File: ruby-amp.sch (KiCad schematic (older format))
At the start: 22 parts, among them J1 AudioJack3_Switch, J2 AudioJack2_Dual_Ground_Switch, P1 10k, P2 100K, P3 1k Lin, Q1 MPF102_DSG, U1 LM386

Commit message: esquematico original listo
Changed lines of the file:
@@
 	5750 3300 5750 2950
 Wire Wire Line
-	5750 2950 5600 2950
+	5750 2950 5650 2950
 Wire Wire Line
 	5600 2950 5600 3050
@@
 	2000 3650 2250 3650
 Connection ~ 2250 3650
+$Comp
+L power:PWR_FLAG #FLG0102
+U 1 1 60BC6256
+P 5650 2850
+F 0 "#FLG0102" H 5650 2925 50  0001 C CNN
+F 1 "PWR_FLAG" H 5650 3023 50  0000 C CNN
+F 2 "" H 5650 2850 50  0001 C CNN
+F 3 "~" H 5650 2850 50  0001 C CNN
+	1    5650 2850
+	1    0    0    -1
+$EndComp
+Wire Wire Line
+	5650 2850 5650 2950
+Connection ~ 5650 2950
+Wire Wire Line
+	5650 2950 5600 2950
 $EndSCHEMATC

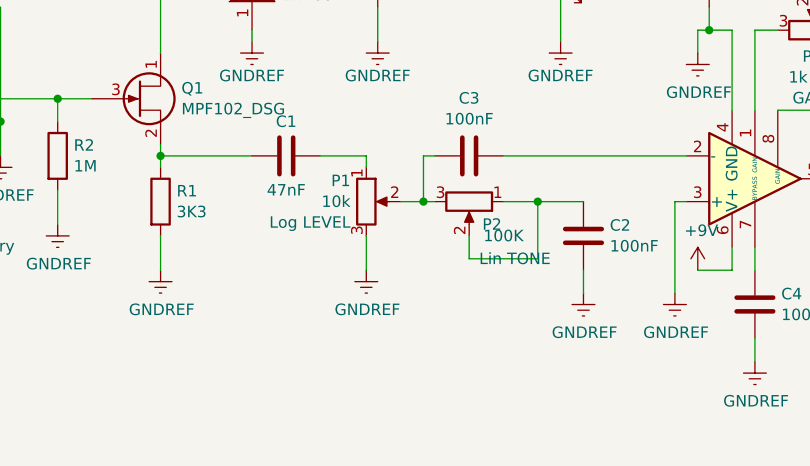
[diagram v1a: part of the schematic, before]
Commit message: footprint listo, netlist listo, PCB empezado
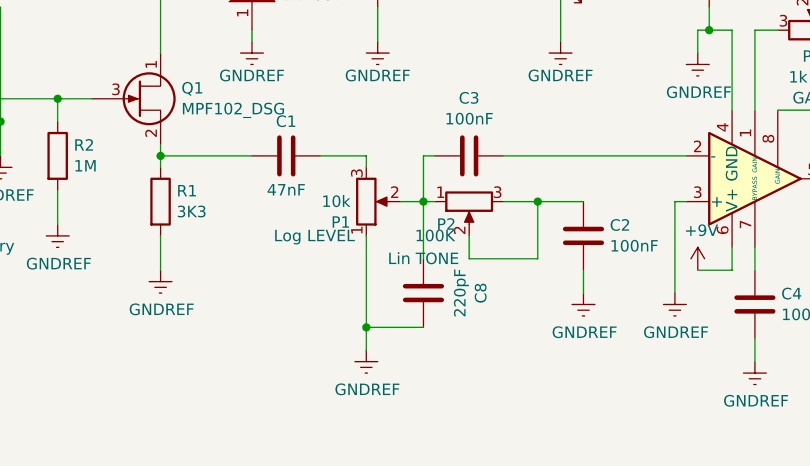
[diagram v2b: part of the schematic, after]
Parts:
- added C8: 220pF, Capacitor_THT:C_Disc_D4.3mm_W1.9mm_P5.00mm, symbol Device:C
- BT1: footprint (none) -> Connector_PinHeader_2.54mm:PinHeader_1x02_P2.54mm_Vertical
- C1: footprint (none) -> Capacitor_THT:C_Disc_D5.1mm_W3.2mm_P5.00mm
- C2, C3, C4, C5: footprint (none) -> Capacitor_THT:C_Disc_D4.3mm_W1.9mm_P5.00mm
- C6, C7: footprint (none) -> Capacitor_THT:CP_Radial_D8.0mm_P5.00mm
- D1: footprint (none) -> Diode_THT:D_A-405_P12.70mm_Horizontal
- D2: footprint (none) -> LED_THT:LED_D5.0mm_Clear
- J1: footprint (none) -> Connector_Audio:Jack_6.35mm_Neutrik_NMJ6HFD4_Horizontal
- J2: footprint (none) -> Connector_Audio:Jack_3.5mm_CUI_SJ1-3533NG_Horizontal
- P1, P2, P3: footprint (none) -> Potentiometer_THT:Potentiometer_Alps_RK09Y11_Single_Horizontal
- Q1: footprint (none) -> Package_TO_SOT_THT:TO-92_Inline
- R1, R2, R3, R4, R5: footprint (none) -> Resistor_THT:R_Axial_DIN0207_L6.3mm_D2.5mm_P10.16mm_Horizontal
- U1: footprint (none) -> Package_DIP:DIP-8_W7.62mm_Socket
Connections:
- net GNDREF: now also P1.1, C8.1; no longer P1.3
- net at C1.1: now also P1.3; no longer P1.1
- net at C3.2, P1.2: now also P2.1, C8.2; no longer P2.3
- net at C2.2, P2.2: now also P2.3; no longer P2.1
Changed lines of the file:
@@
 F 0 "J1" H 2082 3475 50  0000 C CNN
 F 1 "AudioJack3_Switch" H 2082 3384 50  0000 C CNN
-F 2 "" H 2100 3050 50  0001 C CNN
+F 2 "Connector_Audio:Jack_6.35mm_Neutrik_NMJ6HFD4_Horizontal" H 2100 3050 50  0001 C CNN
 F 3 "~" H 2100 3050 50  0001 C CNN
 	1    2100 3050
@@
 F 0 "Q1" H 3341 3296 50  0000 L CNN
 F 1 "MPF102_DSG" H 3341 3205 50  0000 L CNN
-F 2 "" H 3350 3350 50  0001 C CNN
+F 2 "Package_TO_SOT_THT:TO-92_Inline" H 3350 3350 50  0001 C CNN
 F 3 "~" H 3150 3250 50  0001 C CNN
 	1    3150 3250
@@
 F 0 "R2" H 2870 3546 50  0000 L CNN
 F 1 "1M" H 2870 3455 50  0000 L CNN
-F 2 "" V 2730 3500 50  0001 C CNN
+F 2 "Resistor_THT:R_Axial_DIN0207_L6.3mm_D2.5mm_P10.16mm_Horizontal" V 2730 3500 50  0001 C CNN
 F 3 "~" H 2800 3500 50  0001 C CNN
 	1    2800 3500
@@
 F 0 "R1" H 3320 3746 50  0000 L CNN
 F 1 "3K3" H 3320 3655 50  0000 L CNN
-F 2 "" V 3180 3700 50  0001 C CNN
+F 2 "Resistor_THT:R_Axial_DIN0207_L6.3mm_D2.5mm_P10.16mm_Horizontal" V 3180 3700 50  0001 C CNN
 F 3 "~" H 3250 3700 50  0001 C CNN
 	1    3250 3700
@@
 F 0 "C1" V 3650 3500 50  0000 C CNN
 F 1 "47nF" V 3950 3500 50  0000 C CNN
-F 2 "" H 3838 3350 50  0001 C CNN
+F 2 "Capacitor_THT:C_Disc_D5.1mm_W3.2mm_P5.00mm" H 3838 3350 50  0001 C CNN
 F 3 "~" H 3800 3500 50  0001 C CNN
 	1    3800 3500
@@
 F 0 "D1" V 3696 2622 50  0000 R CNN
 F 1 "1N4007" V 3605 2622 50  0000 R CNN
-F 2 "" H 3650 2750 50  0001 C CNN
+F 2 "Diode_THT:D_A-405_P12.70mm_Horizontal" H 3650 2750 50  0001 C CNN
 F 3 "~" H 3650 2750 50  0001 C CNN
 	1    3650 2750
@@
 F 0 "C6" H 4318 2746 50  0000 L CNN
 F 1 "470uF 16V" H 4318 2655 50  0000 L CNN
-F 2 "" H 4238 2550 50  0001 C CNN
+F 2 "Capacitor_THT:CP_Radial_D8.0mm_P5.00mm" H 4238 2550 50  0001 C CNN
 F 3 "~" H 4200 2700 50  0001 C CNN
 	1    4200 2700
@@
 F 0 "R5" V 4493 2400 50  0000 C CNN
 F 1 "560R" V 4584 2400 50  0000 C CNN
-F 2 "" V 4630 2400 50  0001 C CNN
+F 2 "Resistor_THT:R_Axial_DIN0207_L6.3mm_D2.5mm_P10.16mm_Horizontal" V 4630 2400 50  0001 C CNN
 F 3 "~" H 4700 2400 50  0001 C CNN
 	1    4700 2400
@@
 F 0 "D2" V 5039 2532 50  0000 R CNN
 F 1 "LED" V 4948 2532 50  0000 R CNN
-F 2 "" H 5000 2650 50  0001 C CNN
+F 2 "LED_THT:LED_D5.0mm_Clear" H 5000 2650 50  0001 C CNN
 F 3 "~" H 5000 2650 50  0001 C CNN
 	1    5000 2650
@@
 F 0 "C3" V 4348 3500 50  0000 C CNN
 F 1 "100nF" V 4439 3500 50  0000 C CNN
-F 2 "" H 4638 3350 50  0001 C CNN
+F 2 "Capacitor_THT:C_Disc_D4.3mm_W1.9mm_P5.00mm" H 4638 3350 50  0001 C CNN
 F 3 "~" H 4600 3500 50  0001 C CNN
 	1    4600 3500
@@
 F 0 "P1" H 4081 3791 50  0000 R CNN
 F 1 "10k" H 4081 3700 50  0000 R CNN
-F 2 "" H 4150 3700 50  0001 C CNN
+F 2 "Potentiometer_THT:Potentiometer_Alps_RK09Y11_Single_Horizontal" H 4150 3700 50  0001 C CNN
 F 3 "~" H 4150 3700 50  0001 C CNN
-F 4 "Log LEVEL" H 4081 3609 50  0000 R CNN "coment"
+F 4 "Log LEVEL" H 4100 3850 50  0000 R CNN "coment"
 	1    4150 3700
-	1    0    0    -1
+	1    0    0    1
 $EndComp
 $Comp
@@
 F 0 "C2" H 4985 3804 50  0000 R CNN
 F 1 "100nF" H 4985 3895 50  0000 R CNN
-F 2 "" H 5138 3700 50  0001 C CNN
+F 2 "Capacitor_THT:C_Disc_D4.3mm_W1.9mm_P5.00mm" H 5138 3700 50  0001 C CNN
 F 3 "~" H 5100 3850 50  0001 C CNN
 	1    5100 3850
@@
 F 0 "U1" H 6194 3554 50  0000 L CNN
 F 1 "LM386" H 6194 3645 50  0000 L CNN
-F 2 "" H 5950 3700 50  0001 C CNN
+F 2 "Package_DIP:DIP-8_W7.62mm_Socket" H 5950 3700 50  0001 C CNN
 F 3 "http://www.ti.com/lit/ds/symlink/lm386.pdf" H 6050 3800 50  0001 C CNN
 	1    5850 3600
 	1    0    0    1
-$EndComp
-$Comp
-L Device:R_POT P3
-U 1 1 6068ABA5
-P 6100 2950
-F 0 "P3" V 5985 2950 50  0000 C CNN
-F 1 "1k Lin" V 5894 2950 50  0000 C CNN
-F 2 "" H 6100 2950 50  0001 C CNN
-F 3 "~" H 6100 2950 50  0001 C CNN
-F 4 "GAIN" V 5803 2950 50  0000 C CNN "coment"
-	1    6100 2950
-	0    1    -1   0
 $EndComp
 $Comp
@@
 F 0 "C4" H 5735 4104 50  0000 R CNN
 F 1 "100nF" H 5735 4195 50  0000 R CNN
-F 2 "" H 5888 4000 50  0001 C CNN
+F 2 "Capacitor_THT:C_Disc_D4.3mm_W1.9mm_P5.00mm" H 5888 4000 50  0001 C CNN
 F 3 "~" H 5850 4150 50  0001 C CNN
 	1    5850 4150
@@
 F 0 "C5" H 6435 4254 50  0000 R CNN
 F 1 "47nF" H 6435 4345 50  0000 R CNN
-F 2 "" H 6588 4150 50  0001 C CNN
+F 2 "Capacitor_THT:C_Disc_D4.3mm_W1.9mm_P5.00mm" H 6588 4150 50  0001 C CNN
 F 3 "~" H 6550 4300 50  0001 C CNN
 	1    6550 4300
@@
 F 0 "R4" H 7280 4154 50  0000 R CNN
 F 1 "10R" H 7280 4245 50  0000 R CNN
-F 2 "" V 7280 4200 50  0001 C CNN
+F 2 "Resistor_THT:R_Axial_DIN0207_L6.3mm_D2.5mm_P10.16mm_Horizontal" V 7280 4200 50  0001 C CNN
 F 3 "~" H 7350 4200 50  0001 C CNN
 	1    7350 4200
@@
 F 0 "J2" H 7120 3618 50  0000 R CNN
 F 1 "AudioJack2_Dual_Ground_Switch" H 7120 3527 50  0000 R CNN
-F 2 "" H 7300 3800 50  0001 C CNN
+F 2 "Connector_Audio:Jack_3.5mm_CUI_SJ1-3533NG_Horizontal" H 7300 3800 50  0001 C CNN
 F 3 "~" H 7300 3800 50  0001 C CNN
 	1    7350 3600
@@
 F 0 "BT1" H 2142 3804 50  0000 R CNN
 F 1 "Battery" H 2142 3895 50  0000 R CNN
-F 2 "" V 2250 3910 50  0001 C CNN
+F 2 "Connector_PinHeader_2.54mm:PinHeader_1x02_P2.54mm_Vertical" V 2250 3910 50  0001 C CNN
 F 3 "~" V 2250 3910 50  0001 C CNN
 	1    2250 3850
@@
 L power:GNDREF #PWR06
 U 1 1 606A4981
-P 4150 4000
-F 0 "#PWR06" H 4150 3750 50  0001 C CNN
-F 1 "GNDREF" H 4155 3827 50  0000 C CNN
-F 2 "" H 4150 4000 50  0001 C CNN
-F 3 "" H 4150 4000 50  0001 C CNN
-	1    4150 4000
-	1    0    0    -1
-$EndComp
-Wire Wire Line
-	4150 3850 4150 4000
+P 4150 4350
+F 0 "#PWR06" H 4150 4100 50  0001 C CNN
+F 1 "GNDREF" H 4155 4177 50  0000 C CNN
+F 2 "" H 4150 4350 50  0001 C CNN
+F 3 "" H 4150 4350 50  0001 C CNN
+	1    4150 4350
+	1    0    0    -1
+$EndComp
+Wire Wire Line
+	4150 3850 4150 4250
 $Comp
 L power:GNDREF #PWR04
@@
 	6350 3300 5950 3300
 Wire Wire Line
-	6100 2800 6100 2700
-Wire Wire Line
-	6100 2700 6350 2700
-Wire Wire Line
-	6350 2700 6350 2950
-Connection ~ 6350 2950
-Wire Wire Line
 	5850 4000 5850 3900
 $Comp
@@
 F 0 "R3" H 6480 3854 50  0000 R CNN
 F 1 "10R" H 6480 3945 50  0000 R CNN
-F 2 "" V 6480 3900 50  0001 C CNN
+F 2 "Resistor_THT:R_Axial_DIN0207_L6.3mm_D2.5mm_P10.16mm_Horizontal" V 6480 3900 50  0001 C CNN
 F 3 "~" H 6550 3900 50  0001 C CNN
 	1    6550 3900
@@
 F 0 "C7" V 7055 3600 50  0000 C CNN
 F 1 "220 uF 16V" V 6964 3600 50  0000 C CNN
-F 2 "" H 6838 3450 50  0001 C CNN
+F 2 "Capacitor_THT:CP_Radial_D8.0mm_P5.00mm" H 6838 3450 50  0001 C CNN
 F 3 "~" H 6800 3600 50  0001 C CNN
 	1    6800 3600
@@
 F 0 "P2" V 4700 3800 50  0000 C CNN
 F 1 "100K" V 4750 3850 50  0000 C CNN
-F 2 "" H 4600 3700 50  0001 C CNN
+F 2 "Potentiometer_THT:Potentiometer_Alps_RK09Y11_Single_Horizontal" H 4600 3700 50  0001 C CNN
 F 3 "~" H 4600 3700 50  0001 C CNN
 F 4 "Lin TONE" V 4850 3900 50  0000 C CNN "coment"
 	1    4600 3700
-	0    1    1    0
+	0    -1   1    0
 $EndComp
 Wire Wire Line
@@
 Wire Wire Line
 	5650 2950 5600 2950
+$Comp
+L Device:C C8
+U 1 1 60BD04D3
+P 4400 4100
+F 0 "C8" V 4148 4100 50  0000 C CNN
+F 1 "220pF" V 4239 4100 50  0000 C CNN
+F 2 "Capacitor_THT:C_Disc_D4.3mm_W1.9mm_P5.00mm" H 4438 3950 50  0001 C CNN
+F 3 "~" H 4400 4100 50  0001 C CNN
+	1    4400 4100
+	-1   0    0    1
+$EndComp
+Wire Wire Line
+	4400 3950 4400 3700
+Wire Wire Line
+	4400 4250 4150 4250
+Connection ~ 4150 4250
+Wire Wire Line
+	4150 4250 4150 4350
+Connection ~ 6350 2950
+Wire Wire Line
+	6350 2700 6350 2950
+Wire Wire Line
+	6100 2700 6350 2700
+Wire Wire Line
+	6100 2800 6100 2700
+$Comp
+L Device:R_POT P3
+U 1 1 6068ABA5
+P 6100 2950
+F 0 "P3" V 5985 2950 50  0000 C CNN
+F 1 "1k Lin" V 5894 2950 50  0000 C CNN
+F 2 "Potentiometer_THT:Potentiometer_Alps_RK09Y11_Single_Horizontal" H 6100 2950 50  0001 C CNN
+F 3 "~" H 6100 2950 50  0001 C CNN
+F 4 "GAIN" V 5803 2950 50  0000 C CNN "coment"
+	1    6100 2950
+	0    1    -1   0
+$EndComp
 $EndSCHEMATC

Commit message: PCB primera iteración
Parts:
- removed J1: AudioJack3_Switch, Connector_Audio:Jack_6.35mm_Neutrik_NMJ6HFD4_Horizontal, symbol Connector:AudioJack3_Switch
- removed J2: AudioJack2_Dual_Ground_Switch, Connector_Audio:Jack_3.5mm_CUI_SJ1-3533NG_Horizontal, symbol Connector:AudioJack2_Dual_Ground_Switch
- added J1: Input_Signal, Connector_PinHeader_2.54mm:PinHeader_1x03_P2.54mm_Horizontal, symbol Connector:Conn_01x03_Female
- added J2: Output_Signal, Connector_PinHeader_2.54mm:PinHeader_1x03_P2.54mm_Horizontal, symbol Connector:Conn_01x03_Female
- added SW1: SW_DPDT_x2, Button_Switch_THT:SW_CuK_JS202011CQN_DPDT_Straight, symbol Switch:SW_DPDT_x2
- P1, P2, P3: footprint Potentiometer_THT:Potentiometer_Alps_RK09Y11_Single_Horizontal -> Connector_PinHeader_2.54mm:PinHeader_1x03_P2.54mm_Horizontal
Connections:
- net +9V: now also SW1.2 (B); no longer BT1.1 (+)
- net GNDREF: now also J1.1 (Pin_1), J1.2 (Pin_2)
- net at Q1.3 (G), R2.1: now also J1.3 (Pin_3)
- net at R4.2: now also J2.3 (Pin_3)
- net at C7.2: now also J2.1 (Pin_1), J2.2 (Pin_2)
- new net: BT1.1 (+), SW1.1 (A)
- no-connect marks 4 -> 1
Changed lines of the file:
@@
 $EndDescr
-$Comp
-L Connector:AudioJack3_Switch J1
-U 1 1 6067DE76
-P 2100 3050
-F 0 "J1" H 2082 3475 50  0000 C CNN
-F 1 "AudioJack3_Switch" H 2082 3384 50  0000 C CNN
-F 2 "Connector_Audio:Jack_6.35mm_Neutrik_NMJ6HFD4_Horizontal" H 2100 3050 50  0001 C CNN
-F 3 "~" H 2100 3050 50  0001 C CNN
-	1    2100 3050
-	1    0    0    -1
-$EndComp
 $Comp
 L Device:Q_NJFET_DSG Q1
@@
 F 0 "P1" H 4081 3791 50  0000 R CNN
 F 1 "10k" H 4081 3700 50  0000 R CNN
-F 2 "Potentiometer_THT:Potentiometer_Alps_RK09Y11_Single_Horizontal" H 4150 3700 50  0001 C CNN
+F 2 "Connector_PinHeader_2.54mm:PinHeader_1x03_P2.54mm_Horizontal" H 4150 3700 50  0001 C CNN
 F 3 "~" H 4150 3700 50  0001 C CNN
 F 4 "Log LEVEL" H 4100 3850 50  0000 R CNN "coment"
@@
 $EndComp
 $Comp
-L Connector:AudioJack2_Dual_Ground_Switch J2
-U 1 1 60692211
-P 7350 3600
-F 0 "J2" H 7120 3618 50  0000 R CNN
-F 1 "AudioJack2_Dual_Ground_Switch" H 7120 3527 50  0000 R CNN
-F 2 "Connector_Audio:Jack_3.5mm_CUI_SJ1-3533NG_Horizontal" H 7300 3800 50  0001 C CNN
-F 3 "~" H 7300 3800 50  0001 C CNN
-	1    7350 3600
-	-1   0    0    -1
-$EndComp
-$Comp
 L Device:Battery BT1
 U 1 1 6069DECC
@@
 Wire Wire Line
 	6550 3600 6650 3600
-Wire Wire Line
-	7350 4050 7350 3900
 $Comp
 L power:GNDREF #PWR015
@@
 L power:+9V #PWR01
 U 1 1 606C68B6
-P 2000 4150
-F 0 "#PWR01" H 2000 4000 50  0001 C CNN
-F 1 "+9V" H 2015 4323 50  0000 C CNN
-F 2 "" H 2000 4150 50  0001 C CNN
-F 3 "" H 2000 4150 50  0001 C CNN
-	1    2000 4150
+P 1600 4150
+F 0 "#PWR01" H 1600 4000 50  0001 C CNN
+F 1 "+9V" H 1615 4323 50  0000 C CNN
+F 2 "" H 1600 4150 50  0001 C CNN
+F 3 "" H 1600 4150 50  0001 C CNN
+	1    1600 4150
 	1    0    0    -1
 $EndComp
@@
 F 0 "P2" V 4700 3800 50  0000 C CNN
 F 1 "100K" V 4750 3850 50  0000 C CNN
-F 2 "Potentiometer_THT:Potentiometer_Alps_RK09Y11_Single_Horizontal" H 4600 3700 50  0001 C CNN
+F 2 "Connector_PinHeader_2.54mm:PinHeader_1x03_P2.54mm_Horizontal" H 4600 3700 50  0001 C CNN
 F 3 "~" H 4600 3700 50  0001 C CNN
 F 4 "Lin TONE" V 4850 3900 50  0000 C CNN "coment"
@@
 $EndComp
 Wire Wire Line
-	2300 3050 2400 3050
-Wire Wire Line
-	2400 3050 2400 3650
+	2400 3150 2400 3650
 Wire Wire Line
 	2400 3650 2250 3650
-Wire Wire Line
-	2300 3350 2550 3350
-Wire Wire Line
-	2300 2850 2550 2850
-Wire Wire Line
-	2550 2850 2550 3350
-Connection ~ 2550 3350
 $Comp
 L power:GNDREF #PWR0101
@@
 	1    0    0    -1
 $EndComp
-Wire Wire Line
-	2550 3350 2550 3500
-Wire Wire Line
-	2300 3250 2800 3250
 Connection ~ 2800 3250
 Wire Wire Line
-	7150 3400 7050 3400
-Wire Wire Line
-	7050 3400 7050 3600
-Wire Wire Line
-	6950 3600 7050 3600
-Connection ~ 7050 3600
-Wire Wire Line
-	7050 3600 7150 3600
-NoConn ~ 2300 2950
-NoConn ~ 2300 3150
-NoConn ~ 7150 3500
-NoConn ~ 7150 3700
-Wire Wire Line
 	4200 3000 4200 2850
 Wire Wire Line
-	2000 4150 2000 4250
-Wire Wire Line
-	2000 4250 2250 4250
-Wire Wire Line
-	2250 4050 2250 4250
+	1600 4150 1600 4250
 $Comp
 L power:PWR_FLAG #FLG0101
 U 1 1 606F7EE3
-P 1750 4250
-F 0 "#FLG0101" H 1750 4325 50  0001 C CNN
-F 1 "PWR_FLAG" H 1750 4423 50  0000 C CNN
-F 2 "" H 1750 4250 50  0001 C CNN
-F 3 "~" H 1750 4250 50  0001 C CNN
-	1    1750 4250
-	1    0    0    -1
-$EndComp
-Wire Wire Line
-	1750 4250 2000 4250
-Connection ~ 2000 4250
+P 1350 4250
+F 0 "#FLG0101" H 1350 4325 50  0001 C CNN
+F 1 "PWR_FLAG" H 1350 4423 50  0000 C CNN
+F 2 "" H 1350 4250 50  0001 C CNN
+F 3 "~" H 1350 4250 50  0001 C CNN
+	1    1350 4250
+	1    0    0    -1
+$EndComp
+Wire Wire Line
+	1350 4250 1600 4250
 Wire Wire Line
 	5000 3000 5000 2800
@@
 F 0 "P3" V 5985 2950 50  0000 C CNN
 F 1 "1k Lin" V 5894 2950 50  0000 C CNN
-F 2 "Potentiometer_THT:Potentiometer_Alps_RK09Y11_Single_Horizontal" H 6100 2950 50  0001 C CNN
+F 2 "Connector_PinHeader_2.54mm:PinHeader_1x03_P2.54mm_Horizontal" H 6100 2950 50  0001 C CNN
 F 3 "~" H 6100 2950 50  0001 C CNN
 F 4 "GAIN" V 5803 2950 50  0000 C CNN "coment"
@@
 	0    1    -1   0
 $EndComp
+$Comp
+L Connector:Conn_01x03_Female J1
+U 1 1 60C24CDD
+P 2000 3150
+F 0 "J1" H 2200 3200 50  0000 C CNN
+F 1 "Input_Signal" H 2250 3100 50  0000 C CNN
+F 2 "Connector_PinHeader_2.54mm:PinHeader_1x03_P2.54mm_Horizontal" H 2000 3150 50  0001 C CNN
+F 3 "~" H 2000 3150 50  0001 C CNN
+	1    2000 3150
+	-1   0    0    -1
+$EndComp
+Wire Wire Line
+	2550 3050 2550 3500
+Wire Wire Line
+	2400 3150 2200 3150
+Wire Wire Line
+	2200 3250 2800 3250
+Wire Wire Line
+	2550 3050 2200 3050
+Wire Wire Line
+	6950 3600 7200 3600
+Wire Wire Line
+	7350 3500 7200 3500
+Wire Wire Line
+	7200 3500 7200 3600
+Connection ~ 7200 3600
+Wire Wire Line
+	7200 3600 7350 3600
+Wire Wire Line
+	7350 3700 7350 4050
+$Comp
+L Switch:SW_DPDT_x2 SW1
+U 1 1 60C45BDA
+P 2000 4250
+F 0 "SW1" H 2000 4050 50  0000 C CNN
+F 1 "SW_DPDT_x2" H 2000 3950 50  0000 C CNN
+F 2 "Button_Switch_THT:SW_CuK_JS202011CQN_DPDT_Straight" H 2000 4250 50  0001 C CNN
+F 3 "~" H 2000 4250 50  0001 C CNN
+	1    2000 4250
+	1    0    0    -1
+$EndComp
+Wire Wire Line
+	2200 4150 2250 4150
+Wire Wire Line
+	2250 4150 2250 4050
+Wire Wire Line
+	1600 4250 1800 4250
+Connection ~ 1600 4250
+NoConn ~ 2200 4350
+$Comp
+L Connector:Conn_01x03_Female J2
+U 1 1 60C706FF
+P 7550 3600
+F 0 "J2" H 7750 3650 50  0000 C CNN
+F 1 "Output_Signal" H 7800 3550 50  0000 C CNN
+F 2 "Connector_PinHeader_2.54mm:PinHeader_1x03_P2.54mm_Horizontal" H 7550 3600 50  0001 C CNN
+F 3 "~" H 7550 3600 50  0001 C CNN
+	1    7550 3600
+	1    0    0    -1
+$EndComp
 $EndSCHEMATC
